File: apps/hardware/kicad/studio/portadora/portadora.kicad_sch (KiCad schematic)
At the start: 64 parts, among them J1 Teensy 4.1 izq, J10 5V desde USB-C de panel, J11 OUT L 1/4 NRJ3HF-1, J12 OUT R 1/4 NRJ3HF-1, J13 PHONES 3.5 sleeve HP_VGND, J14 CV OUT 3.5, J15 Shield fila 13-5V, J16 Shield fila 12-GND, J2 Teensy 4.1 der, J3 USB host Teensy, J5 Panel IDC 2x15, J6 Raspberry Pi pines 1-10, J7 IN L 1/4 NRJ3HF-1, J8 IN R 1/4 NRJ3HF-1, J9 Audio Shield LINE y HP, SW1 PAD 0 -10 -20 dB, U1 74AHCT1G125, U2 MCP6004

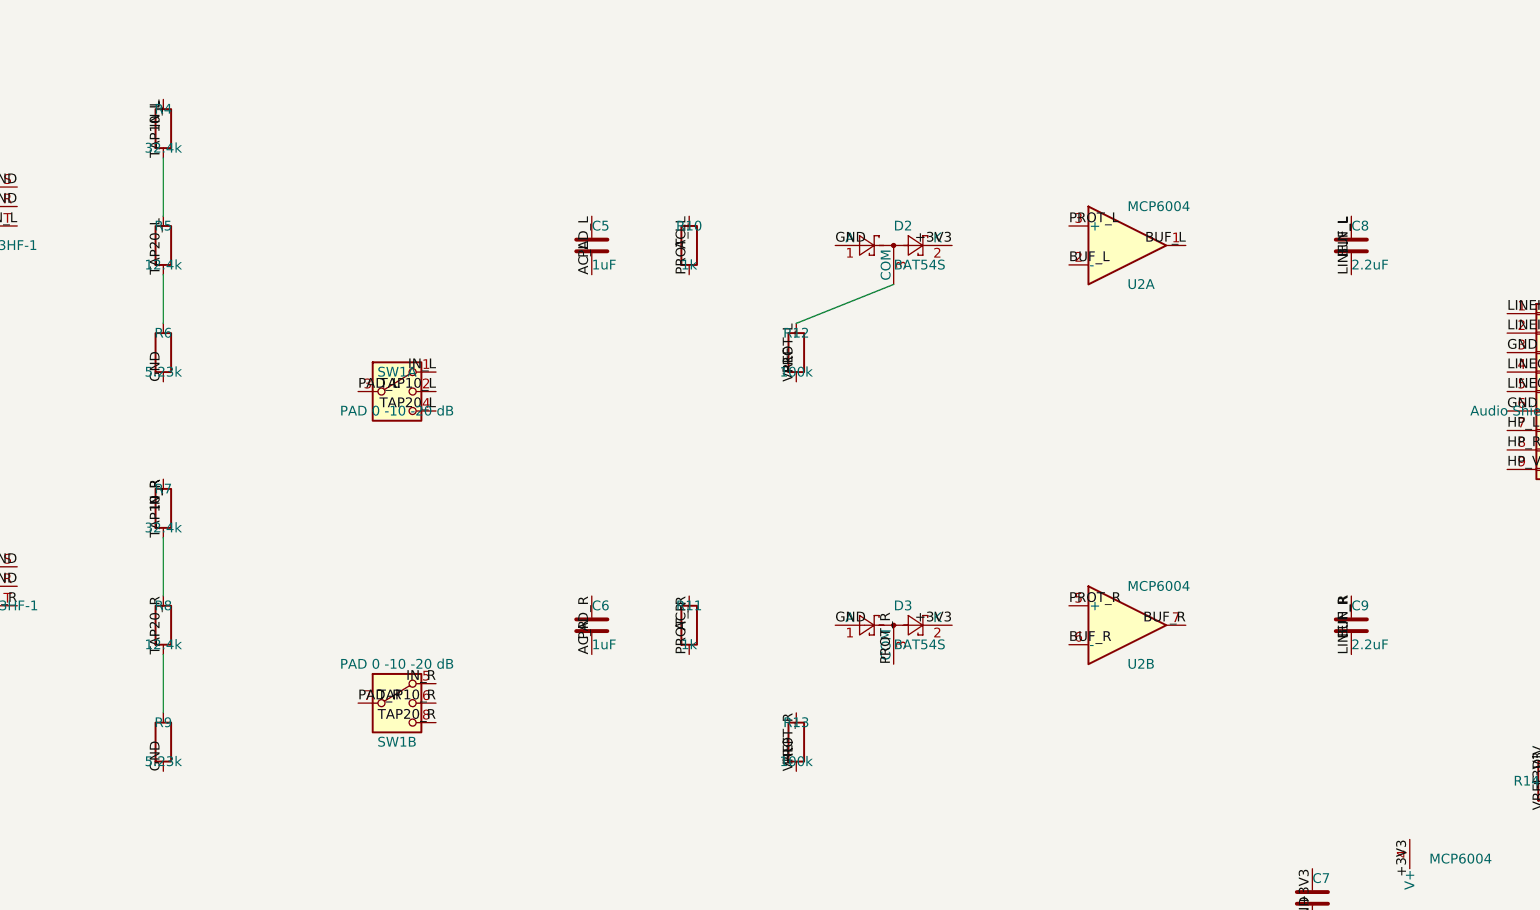
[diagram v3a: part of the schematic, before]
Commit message: feat(hardware): archivos de fabricación JLCPCB y shield corregido en la portadora
- Portadora: las filas del Audio Shield estaban al revés (quedaba espejado respecto de la Teensy con el
  shield boca arriba). J16 (GND/0–12) pasa atrás y J15 adelante; re-ruteada, DRC con paridad 0/0/0.
- Números LCSC en los tres esquemáticos (set_lcsc.py), todo en ensamble Economic. PCB-K pasa al
  SK6812MINI-EA (mismo pinout y cuerpo, sin la restricción Standard-only del MINI-E).
- Escalera del PAD y acople al codec con valores Basic (33k/12k/5.1k, 4.7 µF): la simulación sigue
  pasando C1–C6 (tercera corrida en theory/03).
- export_fab.py: Gerbers + taladros, BOM y CPL en formato JLC; los THT usan el centro de sus pads y los
  IDC la rotación del modelo de JLC. Portadora con jacks e IDC ensamblados; el resto de los THT en
  fab/lcsc-piezas-sueltas.csv.
- sync_fp_fields.py también copia Value y LCSC a las placas.
- theory/02 §10C–10D: fabricación, montaje del shield, J9, J3 (USB host), corriente de la Pi y la
  verificación de punta a punta de las conexiones.

Co-Authored-By: Claude Opus 5.5 <noreply@anthropic.com>
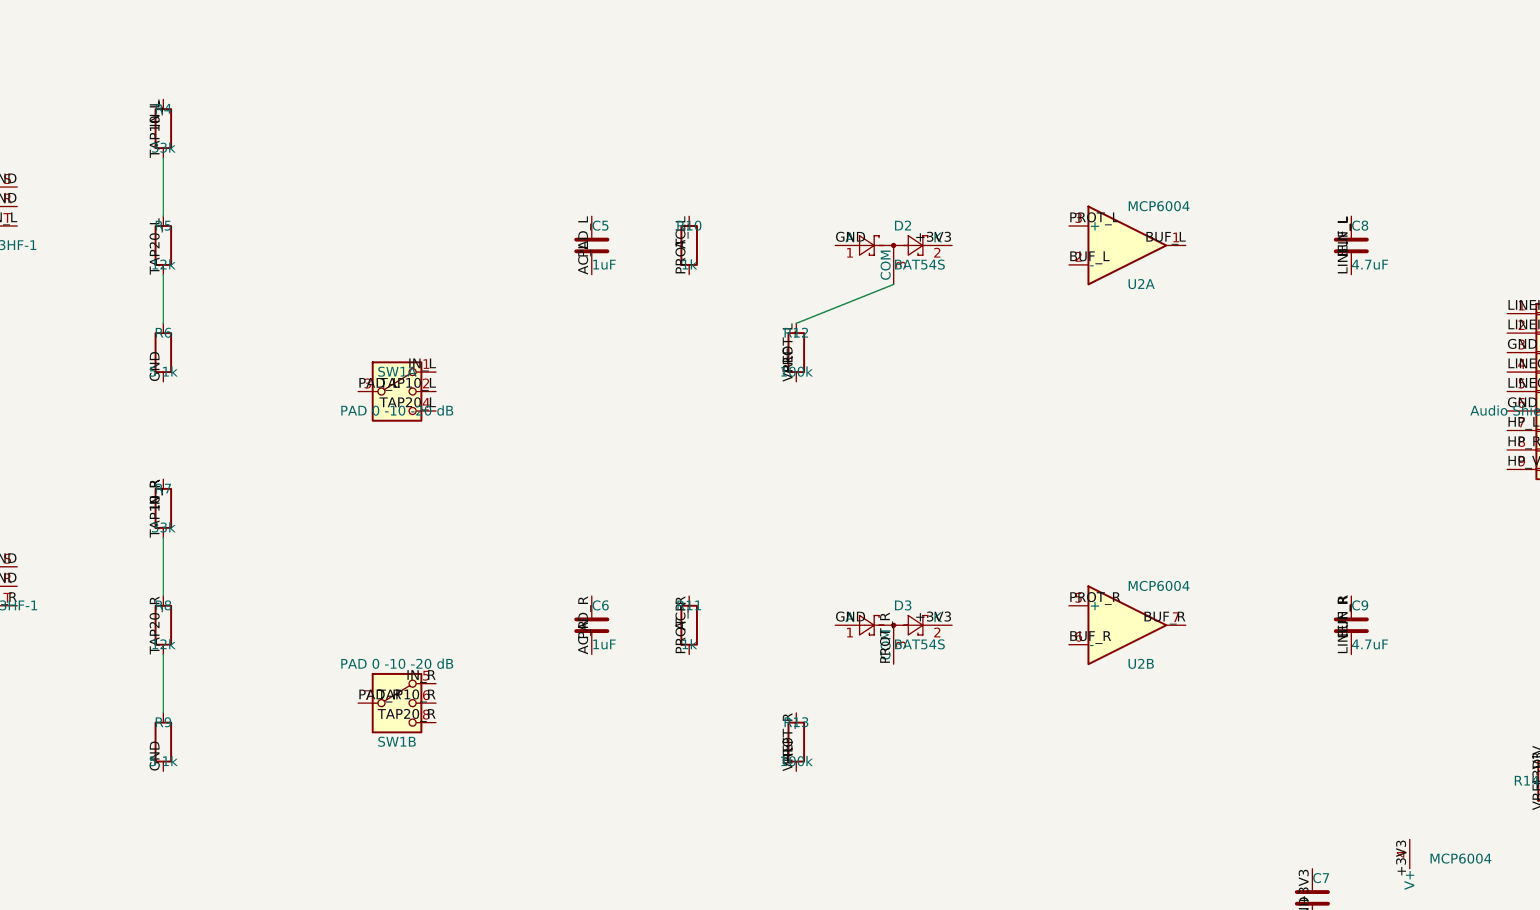
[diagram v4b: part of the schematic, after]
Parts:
- C1: LCSC (none) -> C2992605
- C10, C11, C12, C3: LCSC (none) -> C15850
- C13, C14, C2, C4, C7: LCSC (none) -> C14663
- C5, C6: LCSC (none) -> C28323
- C8, C9: value 2.2uF -> 4.7uF; LCSC (none) -> C1779
- D1: LCSC (none) -> C113975
- D2, D3: LCSC (none) -> C7420333
- F1: LCSC (none) -> C69689
- J11, J12, J7, J8: LCSC (none) -> C22419846
- J13, J14: LCSC (none) -> C4992459
- J5: LCSC (none) -> C48687630
- J6: LCSC (none) -> C492442
- R10, R11, R20: LCSC (none) -> C21190
- R12, R13: LCSC (none) -> C25803
- R14, R15: LCSC (none) -> C25804
- R16, R17: LCSC (none) -> C25819
- R18, R19: LCSC (none) -> C23162
- R3: LCSC (none) -> C23138
- R4, R7: value 32.4k -> 33k; LCSC (none) -> C4216
- R5, R8: value 12.4k -> 12k; LCSC (none) -> C22790
- R6, R9: value 5.23k -> 5.1k; LCSC (none) -> C23186
- U1: LCSC (none) -> C842287
- U2: LCSC (none) -> C7378

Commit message: feat(studio): prototipo económico de 2 placas, enclosure validado en FreeCAD y conectores de chasis
Placas (ADR-004 rev. 3, theory/02 §10F):
- Sin PCB-K ni LEDs montados: los Choc se cablean a J1 de PCB-A, que pasa de JST-SH a header 1×10 acodado
  con el mismo pinout (+5V y LED_DIN libres). PCB-A re-ruteada (build_pcb_a.sh), DRC con paridad 0/0/0.
- Portadora con ensamble solo de SMD; PCB-A solo PCB. export_fab.py genera solo esas dos.
- Todos los conectores traseros de chasis, cableados a los pads de los footprints de jacks (§10H).

Enclosure (apps/design/3d-models/studio, theory/02 §10E–10H):
- Modelo FreeCAD con las placas de KiCad: caja 48/83 a 12°, portadora corrida +16 mm en X para librar el
  GPIO de la Pi con el shield sobre headers.
- Pantalla sujeta con dos barras de PETG a 4 espárragos PEM; aluminio fijado con 6 M3 avellanados.
- Pared trasera en una sola fila (z 22), HOST en USB-A; separadores de la portadora y patas.
- Anillo WS2812 de NAV bajo un difusor Ø44 y soportes impresos para APA102 bajo cada Choc.
- Archivos: cuerpo-petg.stl, barras, soportes de tecla, panel-aluminio.dxf (3 capas), difusor-nav.dxf.

Co-Authored-By: Claude Opus 5.5 <noreply@anthropic.com>
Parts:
- J11, J12, J7, J8: LCSC C22419846 -> (none)
- J13, J14: LCSC C4992459 -> (none)
- J5: LCSC C48687630 -> (none)
- J6: LCSC C492442 -> (none)
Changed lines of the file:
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@@
 			)
 		)
-		(property "LCSC" "C48687630"
-			(at 289.56 110.49 0)
-			(hide yes)
-			(show_name no)
-			(do_not_autoplace no)
-			(effects
-				(font
-					(size 1.27 1.27)
-				)
-			)
-		)
 		(property "Description" "Generic connector, double row, 02x15, odd/even pin numbering scheme (row 1 odd numbers, row 2 even numbers), script generated (kicad-library-utils/schlib/autogen/connector/)"
 			(at 289.56 110.49 0)
@@
 			)
 		)
-		(property "LCSC" "C492442"
-			(at 369.57 74.93 0)
-			(hide yes)
-			(show_name no)
-			(do_not_autoplace no)
-			(effects
-				(font
-					(size 1.27 1.27)
-				)
-			)
-		)
 		(property "Description" "Generic connector, double row, 02x05, odd/even pin numbering scheme (row 1 odd numbers, row 2 even numbers), script generated (kicad-library-utils/schlib/autogen/connector/)"
 			(at 369.57 74.93 0)
@@
 			)
 		)
-		(property "LCSC" "C22419846"
-			(at 25.4 180.34 0)
-			(hide yes)
-			(show_name no)
-			(do_not_autoplace no)
-			(effects
-				(font
-					(size 1.27 1.27)
-				)
-			)
-		)
 		(property "Description" "Audio Jack, 3 Poles (Stereo / TRS)"
 			(at 25.4 180.34 0)
@@
 			)
 		)
-		(property "LCSC" "C22419846"
-			(at 25.4 229.87 0)
-			(hide yes)
-			(show_name no)
-			(do_not_autoplace no)
-			(effects
-				(font
-					(size 1.27 1.27)
-				)
-			)
-		)
 		(property "Description" "Audio Jack, 3 Poles (Stereo / TRS)"
 			(at 25.4 229.87 0)
@@
 			)
 		)
-		(property "LCSC" "C22419846"
-			(at 309.88 180.34 0)
-			(hide yes)
-			(show_name no)
-			(do_not_autoplace no)
-			(effects
-				(font
-					(size 1.27 1.27)
-				)
-			)
-		)
 		(property "Description" "Audio Jack, 3 Poles (Stereo / TRS)"
 			(at 309.88 180.34 0)
@@
 			)
 		)
-		(property "LCSC" "C22419846"
-			(at 309.88 214.63 0)
-			(hide yes)
-			(show_name no)
-			(do_not_autoplace no)
-			(effects
-				(font
-					(size 1.27 1.27)
-				)
-			)
-		)
 		(property "Description" "Audio Jack, 3 Poles (Stereo / TRS)"
 			(at 309.88 214.63 0)
@@
 			)
 		)
-		(property "LCSC" "C4992459"
-			(at 309.88 250.19 0)
-			(hide yes)
-			(show_name no)
-			(do_not_autoplace no)
-			(effects
-				(font
-					(size 1.27 1.27)
-				)
-			)
-		)
 		(property "Description" "Audio Jack, 3 Poles (Stereo / TRS)"
 			(at 309.88 250.19 0)
@@
 			(at 394.97 204.47 0)
 			(hide yes)
-			(show_name no)
-			(do_not_autoplace no)
-			(effects
-				(font
-					(size 1.27 1.27)
-				)
-			)
-		)
-		(property "LCSC" "C4992459"
-			(at 394.97 204.47 0)
-			(hide yes)
